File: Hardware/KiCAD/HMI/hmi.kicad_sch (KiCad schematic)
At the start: 73 parts, among them J1 PJ-307C, J2 PJ-2282, J3 OLED, J4 Conn_01x30, SW1 SW_Push_45deg, SW10 SW_Push_45deg, SW11 SW_Push_45deg, SW12 SW_Push_45deg, SW13 PTT, SW14 ACZ11BRXE, SW15 SW_Push_45deg, SW16 SW_Push_45deg, SW17 SW_Push_45deg, SW18 SW_Push_45deg, SW19 F1, SW2 SW_Push_45deg, SW20 F2, SW3 SW_Push_45deg, SW4 SW_Push_45deg, SW5 SW_Push_45deg, SW6 SW_Push_45deg, SW7 SW_Push_45deg, SW8 SW_Push_45deg, SW9 SW_Push_45deg, U1 MAX9814

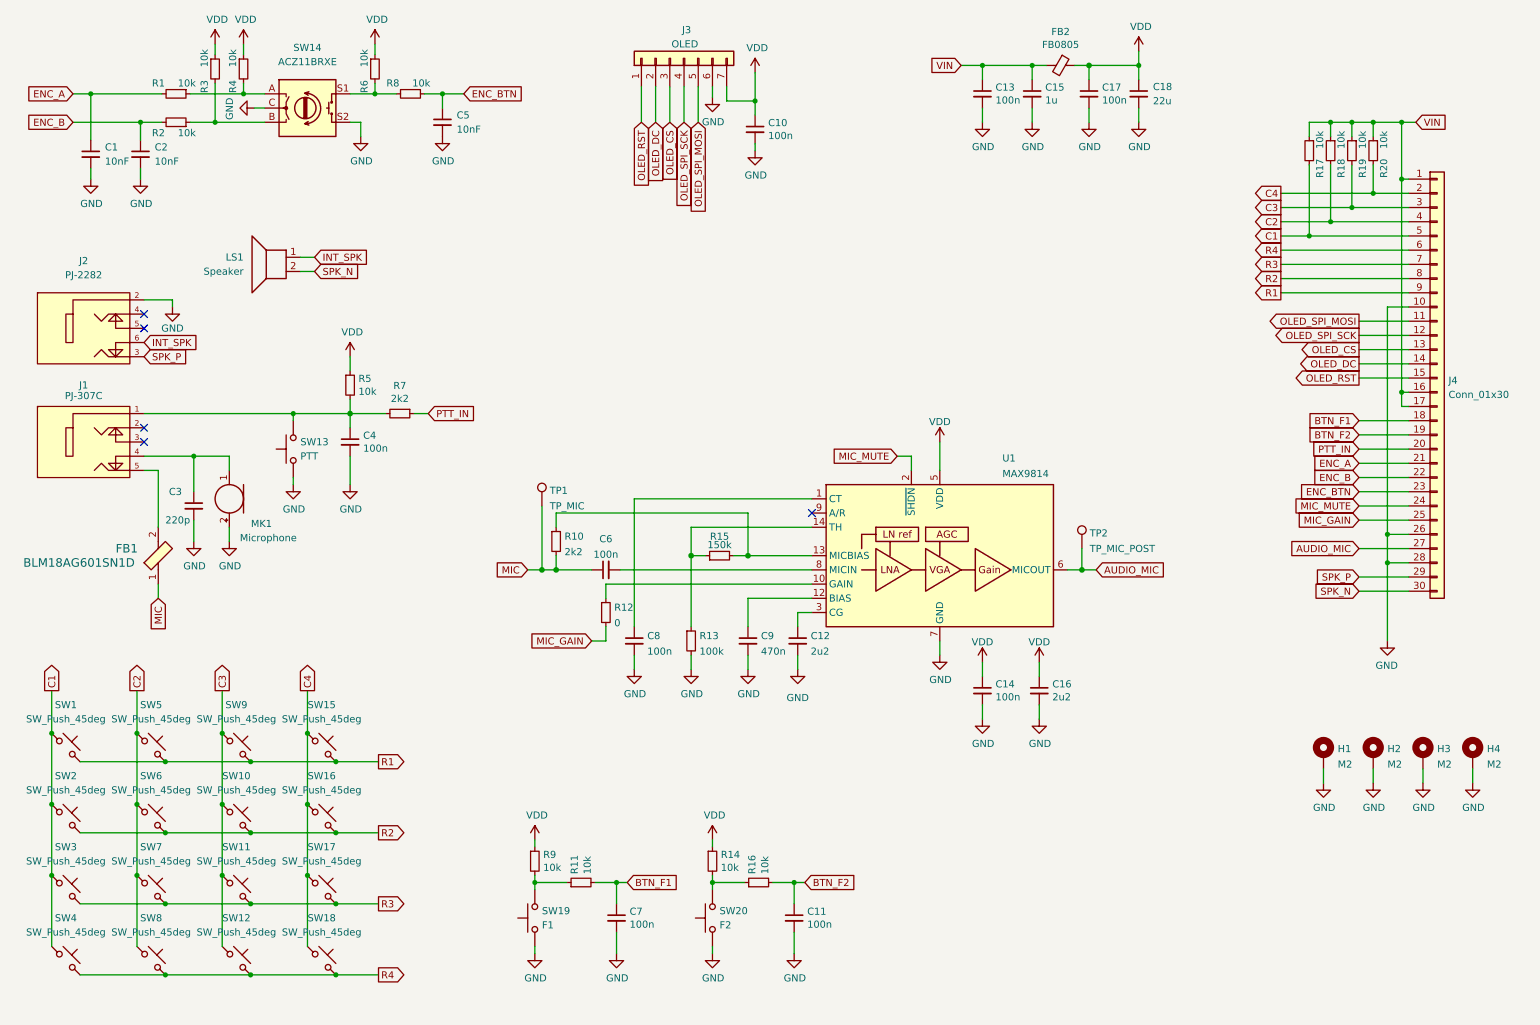
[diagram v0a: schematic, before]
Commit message: SPI for keyboard readout, FPC conn update
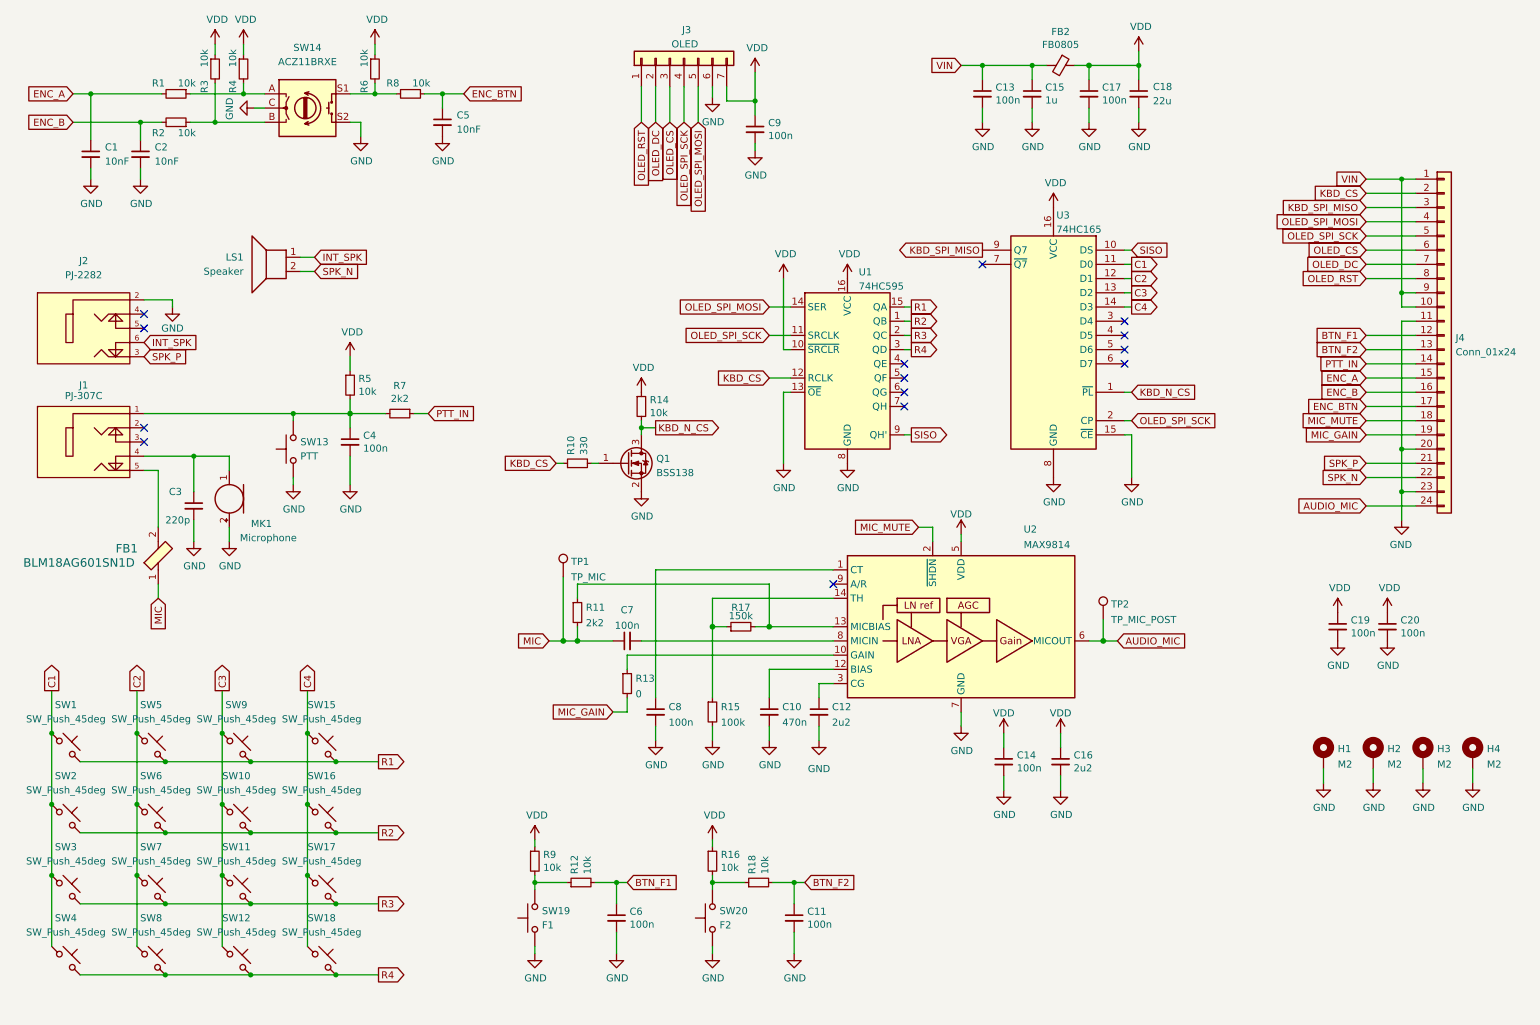
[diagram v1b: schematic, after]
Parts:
- removed J4: Conn_01x30, symbol Connector_Generic:Conn_01x30
- removed R17, R18, R19, R20: 10k, Resistor_SMD:R_0402_1005Metric, symbol pkl_device:pkl_R_Small
- added C19, C20: 100n, Capacitor_SMD:C_0402_1005Metric, symbol pkl_device:pkl_C_Small
- added J4: Conn_01x24, symbol Connector_Generic:Conn_01x24
- added Q1: BSS138, Package_TO_SOT_SMD:SOT-23, symbol Transistor_FET:BSS138
- added R10: 330, Resistor_SMD:R_0402_1005Metric, symbol pkl_device:pkl_R_Small
- added R14: 10k, Resistor_SMD:R_0402_1005Metric, symbol pkl_device:pkl_R_Small
- added U1: 74HC595, Package_SO:SOIC-16_3.9x9.9mm_P1.27mm, symbol 74xx:74HC595
- added U3: 74HC165, Package_SO:SOIC-16_3.9x9.9mm_P1.27mm, symbol 74xx:74HC165
- renumbered C9 to C10, C7 to C6, C6 to C7, C10 to C9, R10 to R11, R11 to R12, R12 to R13, R13 to R15, R14 to R16, R15 to R17, R16 to R18, U1 to U2
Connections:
- net AUDIO_MIC: now also J4.24 (Pin_24)
- net BTN_F1: now also J4.12 (Pin_12)
- net BTN_F2: now also J4.13 (Pin_13)
- net C1: now also U3.11 (D0)
- net C2: now also U3.12 (D1)
- net C3: now also U3.13 (D2)
- net C4: now also U3.14 (D3)
- net ENC_A: now also J4.15 (Pin_15)
- net ENC_B: now also J4.16 (Pin_16)
- net ENC_BTN: now also J4.17 (Pin_17)
- net GND: now also C19.2, C20.2, J4.11 (Pin_11), J4.20 (Pin_20), J4.23 (Pin_23), Q1.2 (S), U1.13 (~{OE}), U1.8 (GND), U3.15 (~{CE}), U3.8 (GND)
- net MIC_GAIN: now also J4.19 (Pin_19)
- net MIC_MUTE: now also J4.18 (Pin_18)
- net OLED_CS: now also J4.6 (Pin_6)
- net OLED_DC: now also J4.7 (Pin_7)
- net OLED_RST: now also J4.8 (Pin_8)
- net OLED_SPI_MOSI: now also J4.4 (Pin_4), U1.14 (SER)
- net OLED_SPI_SCK: now also J4.5 (Pin_5), U1.11 (SRCLK), U3.2 (CP)
- net PTT_IN: now also J4.14 (Pin_14)
- net R1: now also U1.15 (QA)
- net R2: now also U1.1 (QB)
- net R3: now also U1.2 (QC)
- net R4: now also U1.3 (QD)
- net SPK_N: now also J4.22 (Pin_22)
- net SPK_P: now also J4.21 (Pin_21)
- net VDD: now also C19.1, C20.1, R14.1, U1.10 (~{SRCLR}), U1.16 (VCC), U3.16 (VCC)
- net VIN: now also J4.1 (Pin_1), J4.10 (Pin_10), J4.9 (Pin_9)
- new net: Q1.1 (G), R10.2
- new net KBD_CS: J4.2 (Pin_2), R10.1, U1.12 (RCLK)
- new net KBD_N_CS: Q1.3 (D), R14.2, U3.1 (~{PL})
- new net KBD_SPI_MISO: J4.3 (Pin_3), U3.9 (Q7)
- new net SISO: U1.9 (QH'), U3.10 (DS)
- no-connect marks 5 -> 14
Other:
- moved on the sheet: C10, C12, C14, C16, C7, C8, R11, R13, R15, R17, TP1, TP2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

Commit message: add HMI J4 and encoder footprints and change encoder schematic
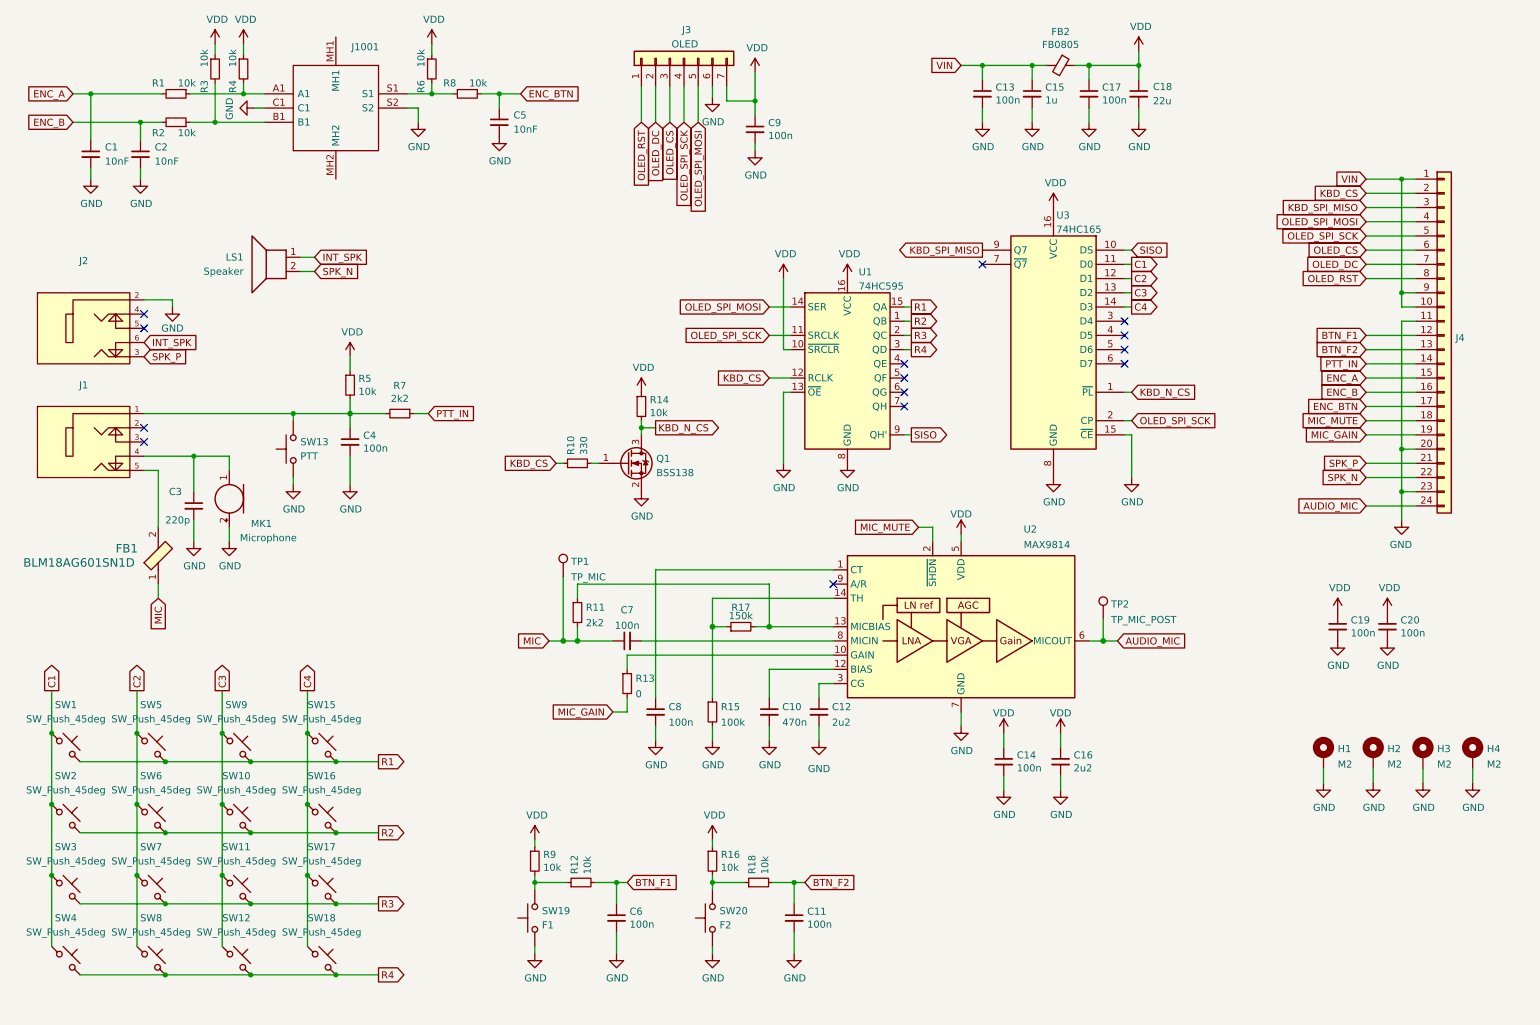
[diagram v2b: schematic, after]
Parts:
- removed SW14: ACZ11BRXE, symbol Device:RotaryEncoder_Switch
- added J1001: (no value), symbol SamacSys_Parts2:ACZ11BR4E-15FA1-20C
- J1: value PJ-307C -> (none)
- J2: value PJ-2282 -> (none)
- J4: value Conn_01x24 -> (none)
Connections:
- net GND: now also J1001.C1, J1001.S2
- net at R2.1, R3.2: now also J1001.B1
- net at R1.1, R4.2: now also J1001.A1
- net at R6.2, R8.2: now also J1001.S1
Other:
- moved on the sheet: C5, R6, R8

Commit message: Add ANY_KEY signal from keypad.
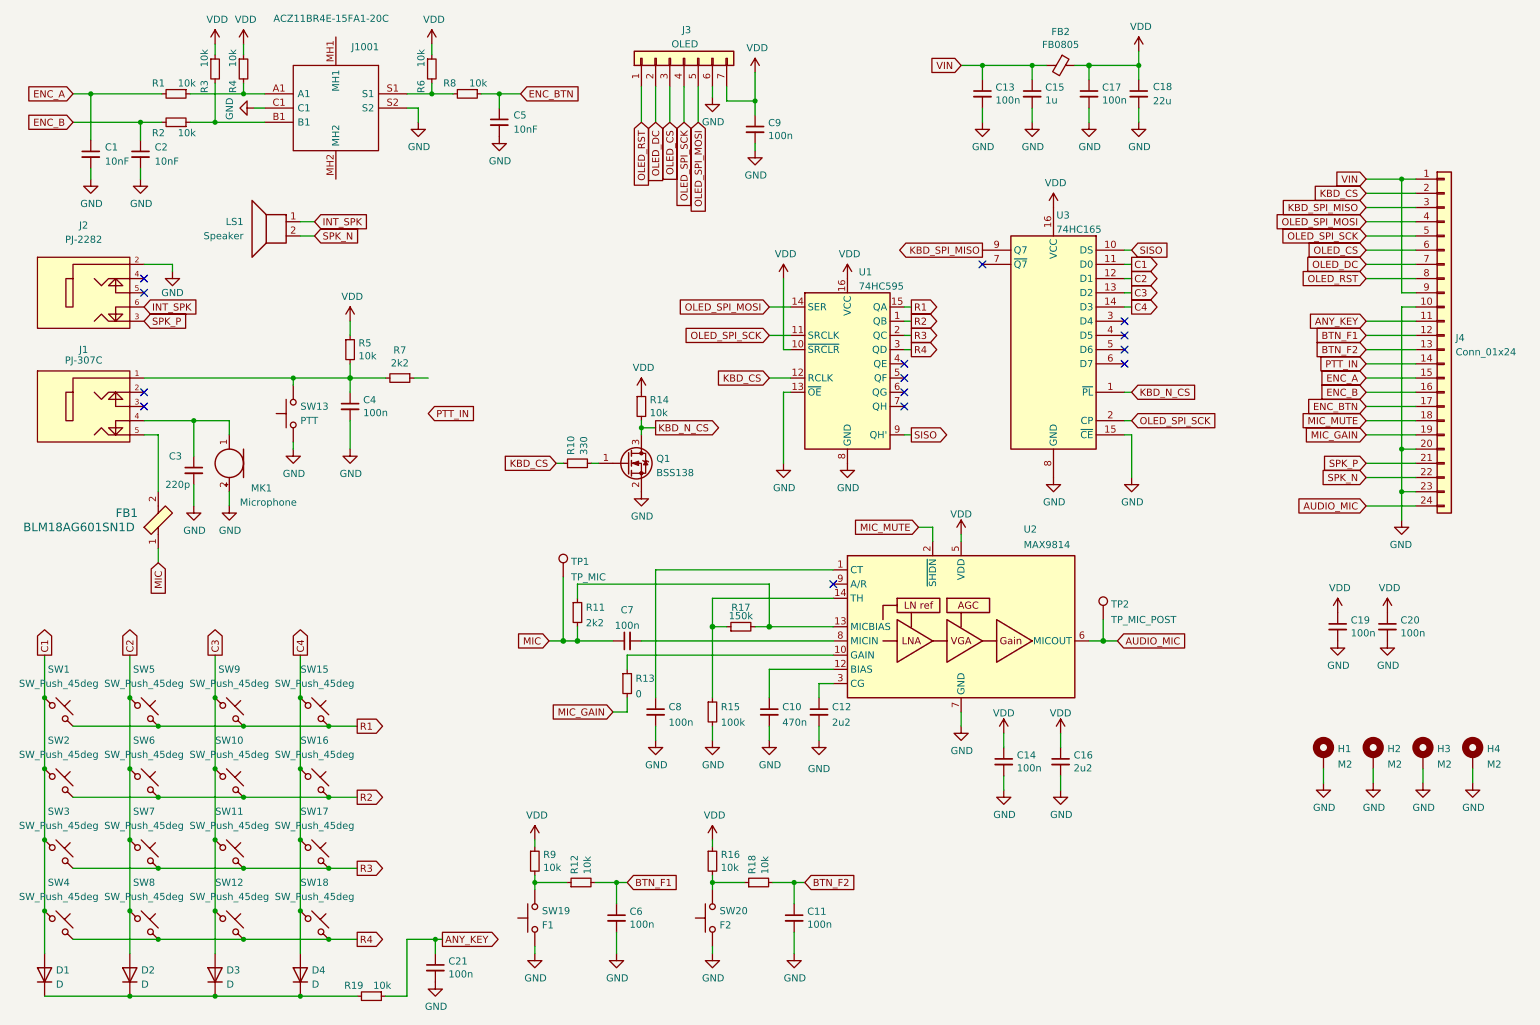
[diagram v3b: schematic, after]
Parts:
- added C21: 100n, Capacitor_SMD:C_0402_1005Metric, symbol pkl_device:pkl_C_Small
- added D1, D2, D3, D4: D, Diode_SMD:D_SOD-923, symbol Device:D
- added R19: 10k, Resistor_SMD:R_0402_1005Metric, symbol pkl_device:pkl_R_Small
- J1: value (none) -> PJ-307C
- J1001: value (none) -> ACZ11BR4E-15FA1-20C; footprint (none) -> SamacSys_Parts2:ACZ11BR4E15FA120C
- J2: value (none) -> PJ-2282
- J4: value (none) -> Conn_01x24; footprint (none) -> Connector_FFC-FPC:Hirose_FH12-24S-0.5SH_1x24-1MP_P0.50mm_Horizontal
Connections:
- net C1: now also D1.2 (A)
- net C2: now also D2.2 (A)
- net C3: now also D3.2 (A)
- net C4: now also D4.2 (A)
- net GND: now also J4.10 (Pin_10), C21.2; no longer J4.11 (Pin_11)
- net PTT_IN: no longer R7.1
- net VIN: no longer J4.10 (Pin_10)
- new net: D1.1 (K), D2.1 (K), D3.1 (K), D4.1 (K), R19.2
- new net ANY_KEY: C21.1, J4.11 (Pin_11), R19.1
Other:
- moved on the sheet: C3, C4, FB1, J1, J2, LS1, MK1, R5, R7, SW1, SW10, SW11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
